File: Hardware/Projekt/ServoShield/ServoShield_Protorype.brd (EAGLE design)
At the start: 100 x 80 mm, 64 parts, among them IC0 74HCT595D, IC1 74HCT595D, IC2 74HCT595D, IC3 74HCT595D, Q1 16MHz

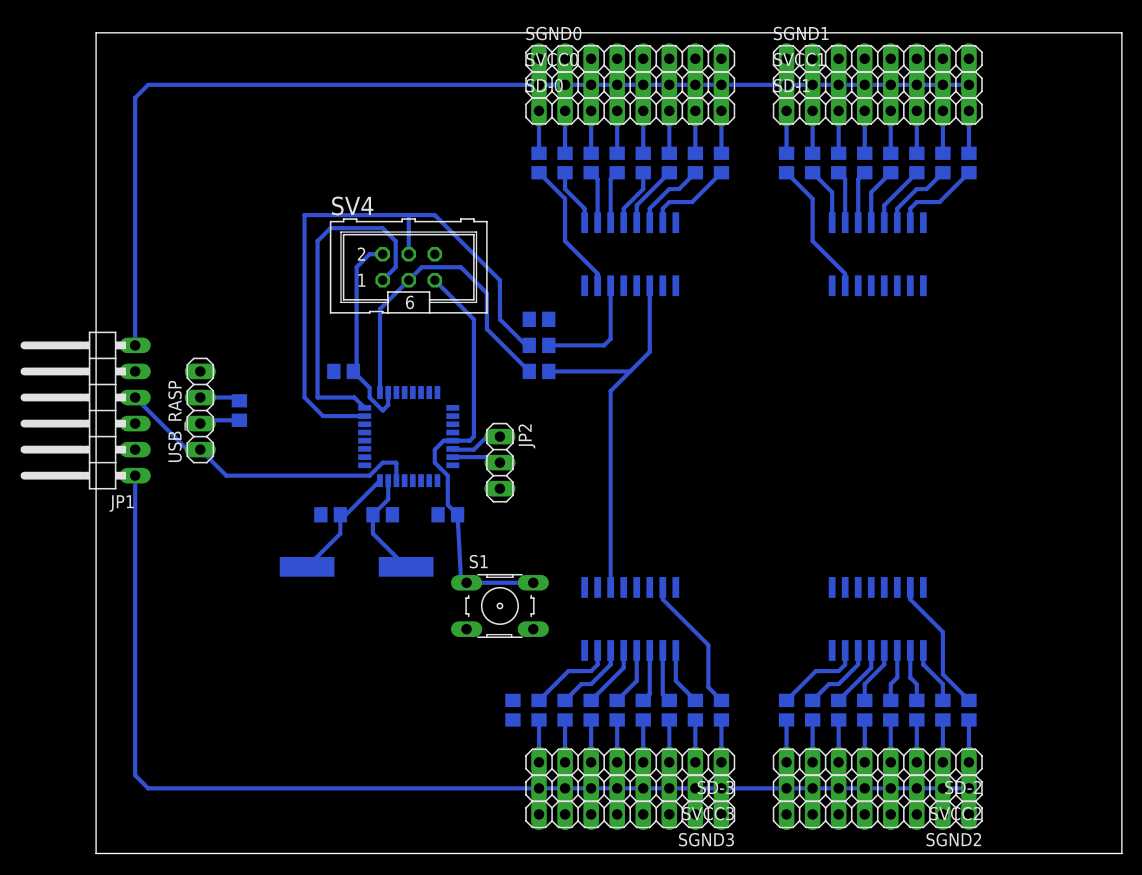
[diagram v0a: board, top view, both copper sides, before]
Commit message: Changed Pinheader and routed all signals
It is not possible to connect 8 servos on one 3x8 pinheader. The servo connectors are to wide. All 3x8 pinheader where changed for 2 3x4 pinheaders.
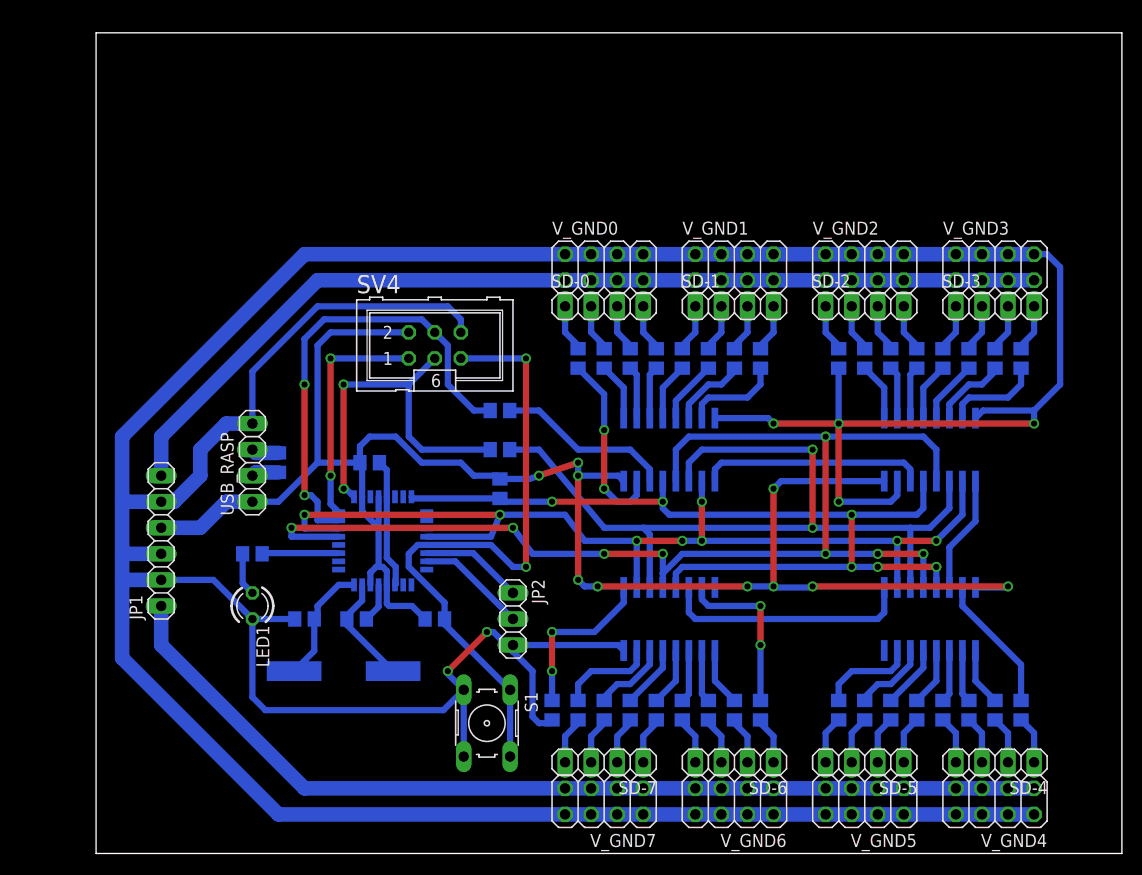
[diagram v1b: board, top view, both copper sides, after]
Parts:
- removed SGND0, SGND1, SGND2, SGND3, SVCC0, SVCC1, SVCC2, SVCC3: (no value), pinhead:1X08
- added LED1: GN_2V, led:LED3MM
- added R39: 1k5, rcl:R0805
- added SD-4, SD-5, SD-6, SD-7: (no value), pinhead:1X04
- added V_GND0, V_GND1, V_GND2, V_GND3, V_GND4, V_GND5, V_GND6, V_GND7: (no value), pinhead:2X04
- JP1: device pinhead:1X06/90 -> pinhead:1X06
- SD-0, SD-1, SD-2, SD-3: device pinhead:1X08 -> pinhead:1X04
- moved SD-3 56.9 mm to (87.6, 53.3), turned to 0 degrees
- moved SD-2 44.5 mm to (74.9, 53.3), turned to 0 degrees
- moved SD-1 23.6 mm to (62.2, 53.3)
- moved R16 19.7 mm to (74.9, 48.3)
- moved IC1 19.7 mm to (81.3, 39.4)
- moved R15 19.7 mm to (72.4, 48.3)
- moved R17 19.7 mm to (77.5, 48.3)
- moved R18 19.7 mm to (80.0, 48.3)
- moved R19 19.7 mm to (82.5, 48.3)
- moved R20 19.7 mm to (85.1, 48.3)
- moved R21 19.7 mm to (87.6, 48.3)
- moved R22 19.7 mm to (90.2, 48.3)
- moved IC0 19.4 mm to (55.9, 39.4)
- moved R10 19.4 mm to (54.6, 48.3)
- moved R7 19.4 mm to (47.0, 48.3)
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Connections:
- removed net N$23: ATMEGA328.24
- new net LED: ATMEGA328.11, R39.1
- new net N$85: LED1.A, R39.2
- net +5V/1: now also V_GND0.1, V_GND0.3, V_GND0.5, V_GND0.7, V_GND1.1, V_GND1.3, V_GND1.5, V_GND1.7, V_GND2.1, V_GND2.3, V_GND2.5, V_GND2.7, V_GND3.1, V_GND3.3, V_GND3.5, V_GND3.7; no longer SVCC0.1, SVCC0.2, SVCC0.3, SVCC0.4, SVCC0.5, SVCC0.6, SVCC0.7, SVCC0.8, SVCC1.1, SVCC1.2, SVCC1.3, SVCC1.4, SVCC1.5, SVCC1.6, SVCC1.7, SVCC1.8
- net +5V/2: now also V_GND4.1, V_GND4.3, V_GND4.5, V_GND4.7, V_GND5.1, V_GND5.3, V_GND5.5, V_GND5.7, V_GND6.1, V_GND6.3, V_GND6.5, V_GND6.7, V_GND7.1, V_GND7.3, V_GND7.5, V_GND7.7; no longer SVCC2.1, SVCC2.2, SVCC2.3, SVCC2.4, SVCC2.5, SVCC2.6, SVCC2.7, SVCC2.8, SVCC3.1, SVCC3.2, SVCC3.3, SVCC3.4, SVCC3.5, SVCC3.6, SVCC3.7, SVCC3.8
- net G: now also ATMEGA328.24; no longer ATMEGA328.12
- net GND: now also LED1.K, V_GND0.2, V_GND0.4, V_GND0.6, V_GND0.8, V_GND1.2, V_GND1.4, V_GND1.6, V_GND1.8, V_GND2.2, V_GND2.4, V_GND2.6, V_GND2.8, V_GND3.2, V_GND3.4, V_GND3.6, V_GND3.8, V_GND4.2, V_GND4.4, V_GND4.6, V_GND4.8, V_GND5.2, V_GND5.4, V_GND5.6, V_GND5.8, V_GND6.2, V_GND6.4, V_GND6.6, V_GND6.8, V_GND7.2, V_GND7.4, V_GND7.6, V_GND7.8; no longer SGND0.1, SGND0.2, SGND0.3, SGND0.4, SGND0.5, SGND0.6, SGND0.7, SGND0.8, SGND1.1, SGND1.2, SGND1.3, SGND1.4, SGND1.5, SGND1.6, SGND1.7, SGND1.8, SGND2.1, SGND2.2, SGND2.3, SGND2.4, SGND2.5, SGND2.6, SGND2.7, SGND2.8, SGND3.1, SGND3.2, SGND3.3, SGND3.4, SGND3.5, SGND3.6, SGND3.7, SGND3.8
- net N$29: now also SD-1.1; no longer SD-0.5
- net N$30: now also SD-1.2; no longer SD-0.6
- net N$31: now also SD-1.3; no longer SD-0.7
- net N$32: now also SD-1.4; no longer SD-0.8
- net N$34: now also SD-2.1; no longer SD-1.1
- net N$43: now also SD-2.2; no longer SD-1.2
- net N$44: now also SD-2.3; no longer SD-1.3
- net N$45: now also SD-2.4; no longer SD-1.4
- net N$46: now also SD-3.1; no longer SD-1.5
- net N$47: now also SD-3.2; no longer SD-1.6
- net N$48: now also SD-3.3; no longer SD-1.7
- net N$49: now also SD-3.4; no longer SD-1.8
- net N$60: now also SD-4.1; no longer SD-2.1
- net N$61: now also SD-4.2; no longer SD-2.2
- net N$62: now also SD-4.3; no longer SD-2.3
- net N$63: now also SD-4.4; no longer SD-2.4
- net N$64: now also SD-5.1; no longer SD-2.5
- net N$65: now also SD-5.2; no longer SD-2.6
- net N$66: now also SD-5.3; no longer SD-2.7
- net N$67: now also SD-5.4; no longer SD-2.8
- net N$76: now also SD-6.1; no longer SD-3.1
- net N$77: now also SD-6.2; no longer SD-3.2
- net N$78: now also SD-6.3; no longer SD-3.3
- net N$79: now also SD-6.4; no longer SD-3.4
- net N$80: now also SD-7.1; no longer SD-3.5
- net N$81: now also SD-7.2; no longer SD-3.6
- net N$82: now also SD-7.3; no longer SD-3.7
- net N$83: now also SD-7.4; no longer SD-3.8
- net N$9: now also ATMEGA328.12; no longer ATMEGA328.11
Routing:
- net GND: track 0.00 -> 423.9 mm, vias 0 -> 4
- net VCC: track 51.2 -> 175.0 mm, vias 0 -> 10
- net RCK: track 0.00 -> 119.7 mm, vias 0 -> 8
- net SCL: track 0.00 -> 97.9 mm, vias 0 -> 8
- net G: track 0.00 -> 90.0 mm, vias 0 -> 6
- net SCK1: track 38.9 -> 83.8 mm, vias 0 -> 2
- net N$53: track 0.00 -> 24.5 mm
- net N$36: track 0.00 -> 21.9 mm
- net !RST: track 41.8 -> 63.2 mm, vias 0 -> 2
- net +5V/2: track 111.0 -> 94.7 mm
- net N$52: track 0.00 -> 16.3 mm, vias 0 -> 2
- net MOSI: track 57.6 -> 45.4 mm, vias 0 -> 2
- net N$5: track 0.00 -> 11.4 mm
- net +5V/1: track 105.9 -> 95.2 mm
- net MISO: track 33.3 -> 22.9 mm, vias 0 -> 2
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
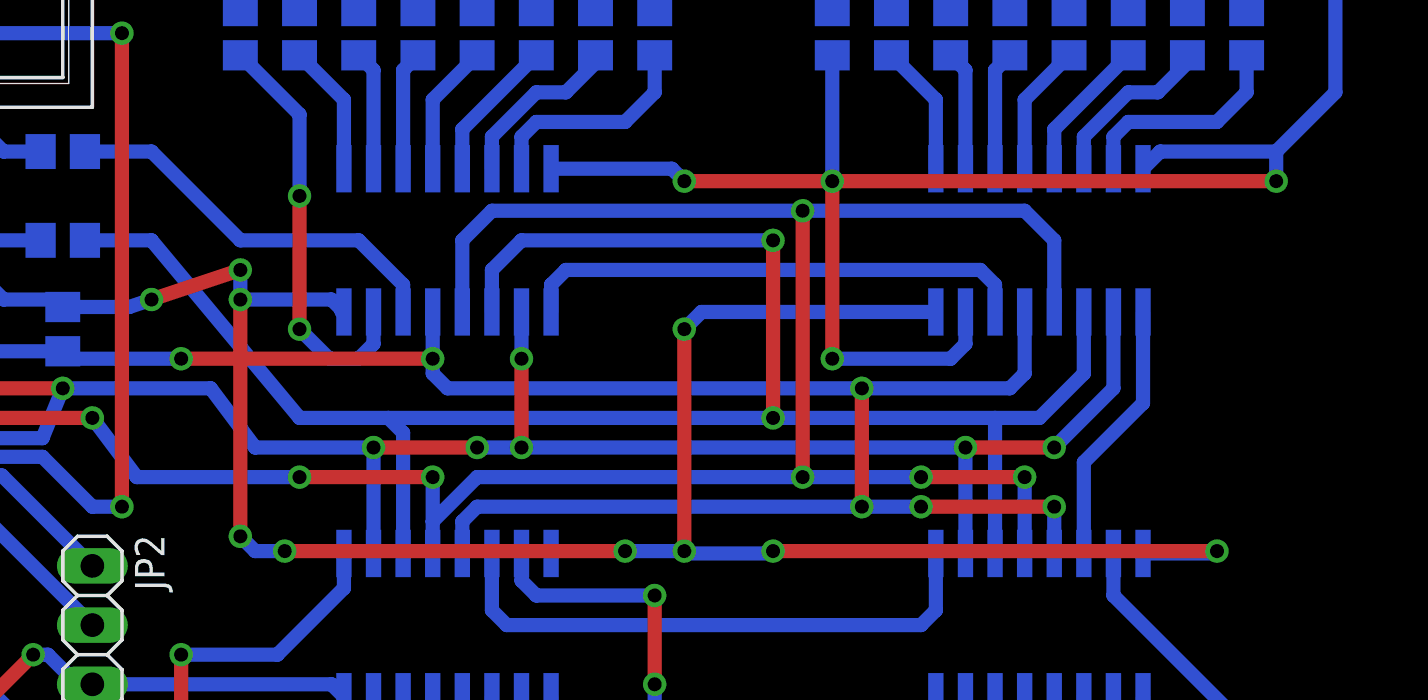
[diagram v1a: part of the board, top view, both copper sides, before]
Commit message: Corrected some overlapping routes
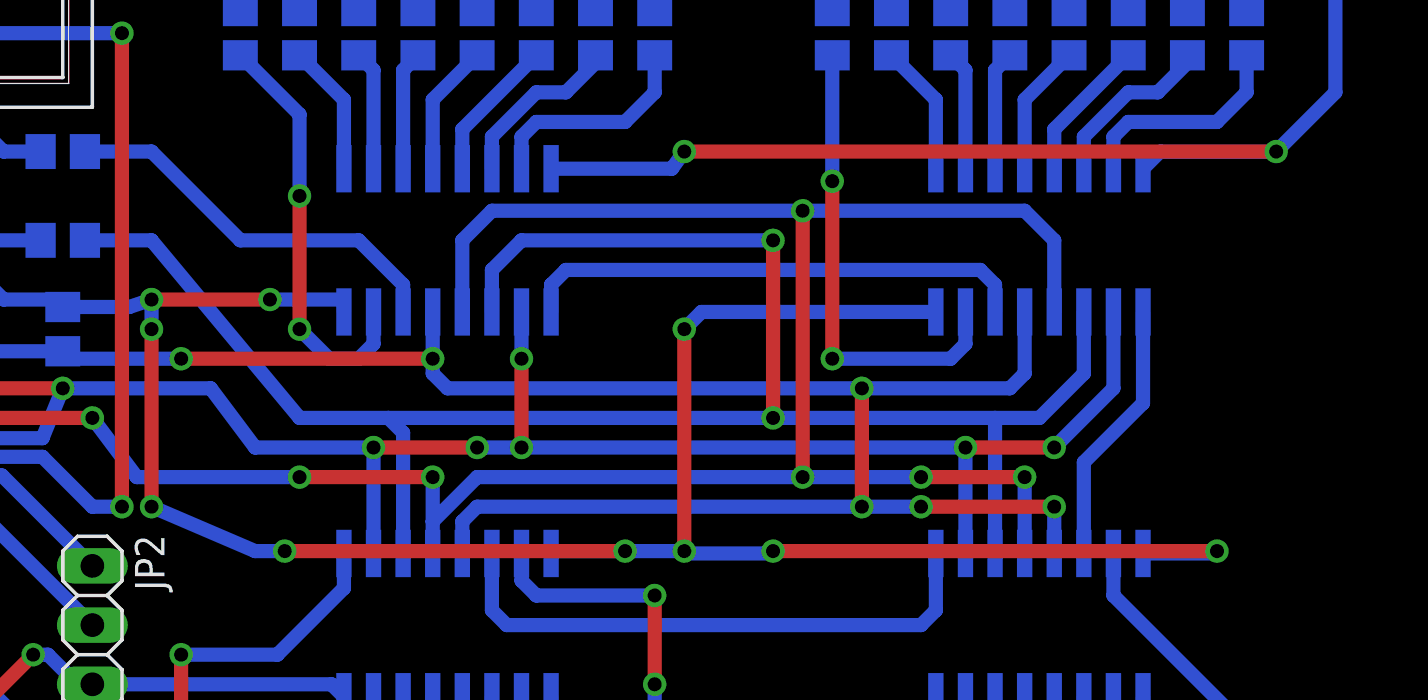
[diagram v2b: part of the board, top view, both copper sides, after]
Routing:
- net VCC: track 175.0 -> 179.7 mm
- net GND: track 423.9 -> 422.8 mm
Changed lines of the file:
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@@
 <wire x1="15.24" y1="46.99" x2="15.24" y2="41.91" width="0.6096" layer="16"/>
 <wire x1="60.325" y1="42.4434" x2="65.5066" y2="42.4434" width="0.6096" layer="16"/>
-<wire x1="65.5066" y1="42.4434" x2="66.04" y2="41.91" width="0.6096" layer="16"/>
-<via x="66.04" y="41.91" extent="1-16" drill="0.6" shape="octagon"/>
-<wire x1="91.44" y1="43.18" x2="91.44" y2="41.91" width="0.6096" layer="16"/>
-<via x="91.44" y="41.91" extent="1-16" drill="0.6" shape="octagon"/>
-<wire x1="66.04" y1="41.91" x2="91.44" y2="41.91" width="0.6096" layer="1"/>
+<wire x1="65.5066" y1="42.4434" x2="66.04" y2="43.18" width="0.6096" layer="16"/>
+<via x="66.04" y="43.18" extent="1-16" drill="0.6" shape="octagon"/>
+<via x="91.44" y="43.18" extent="1-16" drill="0.6" shape="octagon"/>
+<wire x1="66.04" y1="43.18" x2="91.44" y2="43.18" width="0.6096" layer="1"/>
 <wire x1="76.2" y1="3.81" x2="76.835" y2="19.7866" width="0" layer="19" extent="16-16"/>
 <wire x1="26.35" y1="22.86" x2="19.37" y2="22.86" width="0" layer="19" extent="16-16"/>
@@
 <wire x1="26.67" y1="40.64" x2="25.72" y2="39.69" width="0.6096" layer="16"/>
 <wire x1="25.72" y1="39.69" x2="25.72" y2="38.1" width="0.6096" layer="16"/>
-<wire x1="51.435" y1="36.2966" x2="51.3334" y2="36.2966" width="0.6096" layer="16"/>
 <wire x1="39.37" y1="36.51" x2="42.225" y2="36.51" width="0.6096" layer="16"/>
 <wire x1="42.225" y1="36.51" x2="43.18" y2="36.83" width="0.6096" layer="16"/>
 <via x="43.18" y="36.83" extent="1-16" drill="0.6" shape="octagon"/>
-<via x="46.99" y="38.1" extent="1-16" drill="0.6" shape="octagon"/>
-<wire x1="43.18" y1="36.83" x2="46.99" y2="38.1" width="0.6096" layer="1"/>
+<via x="48.26" y="36.83" extent="1-16" drill="0.6" shape="octagon"/>
+<wire x1="43.18" y1="36.83" x2="48.26" y2="36.83" width="0.6096" layer="1"/>
 <wire x1="69.7484" y1="25.9334" x2="69.85" y2="26.035" width="0.6096" layer="16"/>
 <wire x1="85.725" y1="25.9334" x2="88.7984" y2="25.9334" width="0.6096" layer="16"/>
@@
 <via x="48.895" y="26.035" extent="1-16" drill="0.6" shape="octagon"/>
 <wire x1="48.895" y1="26.035" x2="47.625" y2="26.035" width="0.6096" layer="16"/>
-<wire x1="47.625" y1="26.035" x2="46.99" y2="26.67" width="0.6096" layer="16"/>
-<via x="46.99" y="26.67" extent="1-16" drill="0.6" shape="octagon"/>
-<wire x1="46.99" y1="26.67" x2="46.99" y2="36.83" width="0.6096" layer="1"/>
-<via x="46.99" y="36.83" extent="1-16" drill="0.6" shape="octagon"/>
-<wire x1="46.99" y1="36.83" x2="50.9016" y2="36.83" width="0.6096" layer="16"/>
-<wire x1="50.9016" y1="36.83" x2="51.435" y2="36.2966" width="0.6096" layer="16"/>
-<wire x1="46.99" y1="38.1" x2="46.99" y2="36.83" width="0.6096" layer="16"/>
-<wire x1="63.5" y1="26.035" x2="60.325" y2="25.9334" width="0" layer="19" extent="16-16"/>
+<wire x1="47.625" y1="26.035" x2="43.18" y2="27.94" width="0.6096" layer="16"/>
+<via x="43.18" y="27.94" extent="1-16" drill="0.6" shape="octagon"/>
+<wire x1="43.18" y1="27.94" x2="43.18" y2="35.56" width="0.6096" layer="1"/>
+<via x="43.18" y="35.56" extent="1-16" drill="0.6" shape="octagon"/>
+<wire x1="63.5" y1="26.035" x2="60.325" y2="26.035" width="0.6096" layer="16"/>
+<wire x1="60.325" y1="26.035" x2="60.325" y2="25.9334" width="0.6096" layer="16"/>
+<wire x1="43.18" y1="35.56" x2="43.18" y2="36.83" width="0.6096" layer="16"/>
+<wire x1="48.26" y1="36.83" x2="51.435" y2="36.83" width="0.6096" layer="16"/>
+<wire x1="51.435" y1="36.83" x2="51.435" y2="36.2966" width="0.6096" layer="16"/>
 </signal>
 <signal name="N$1">

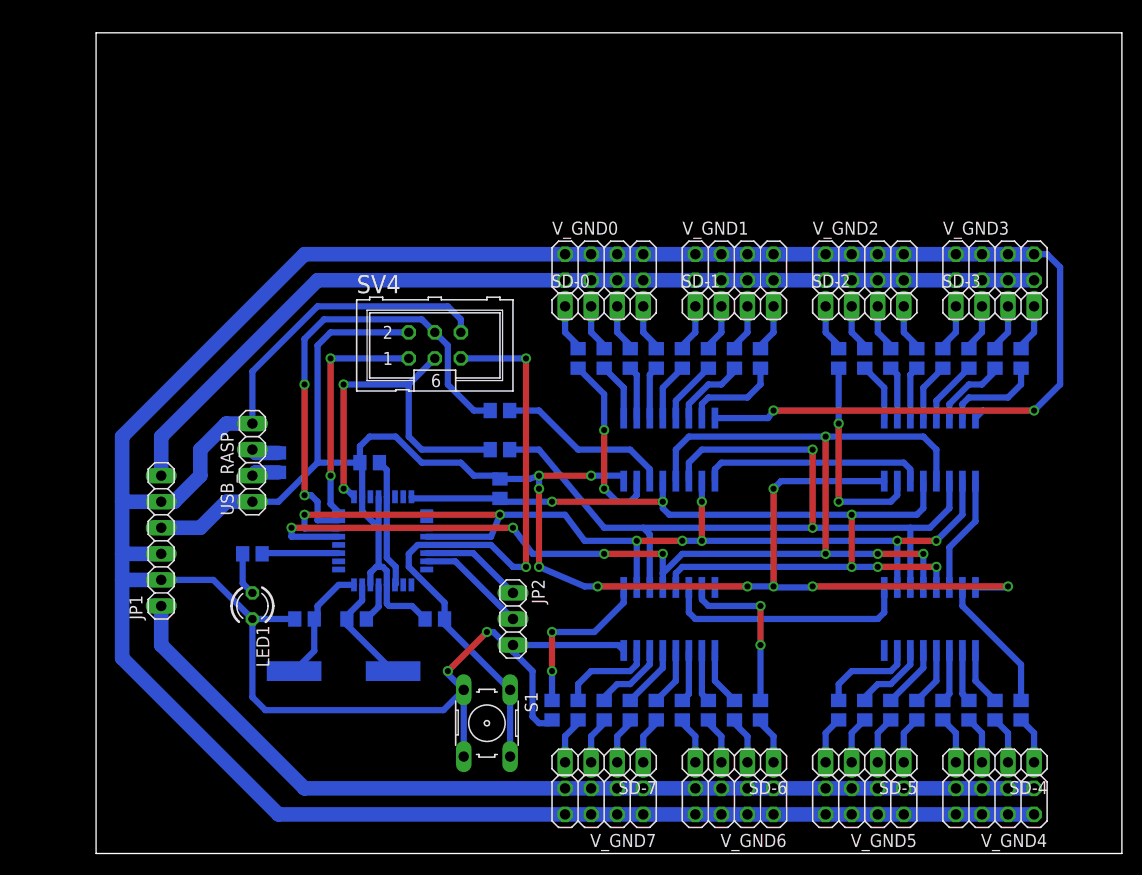
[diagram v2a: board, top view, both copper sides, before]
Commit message: Changed via diameter and routed missing signals
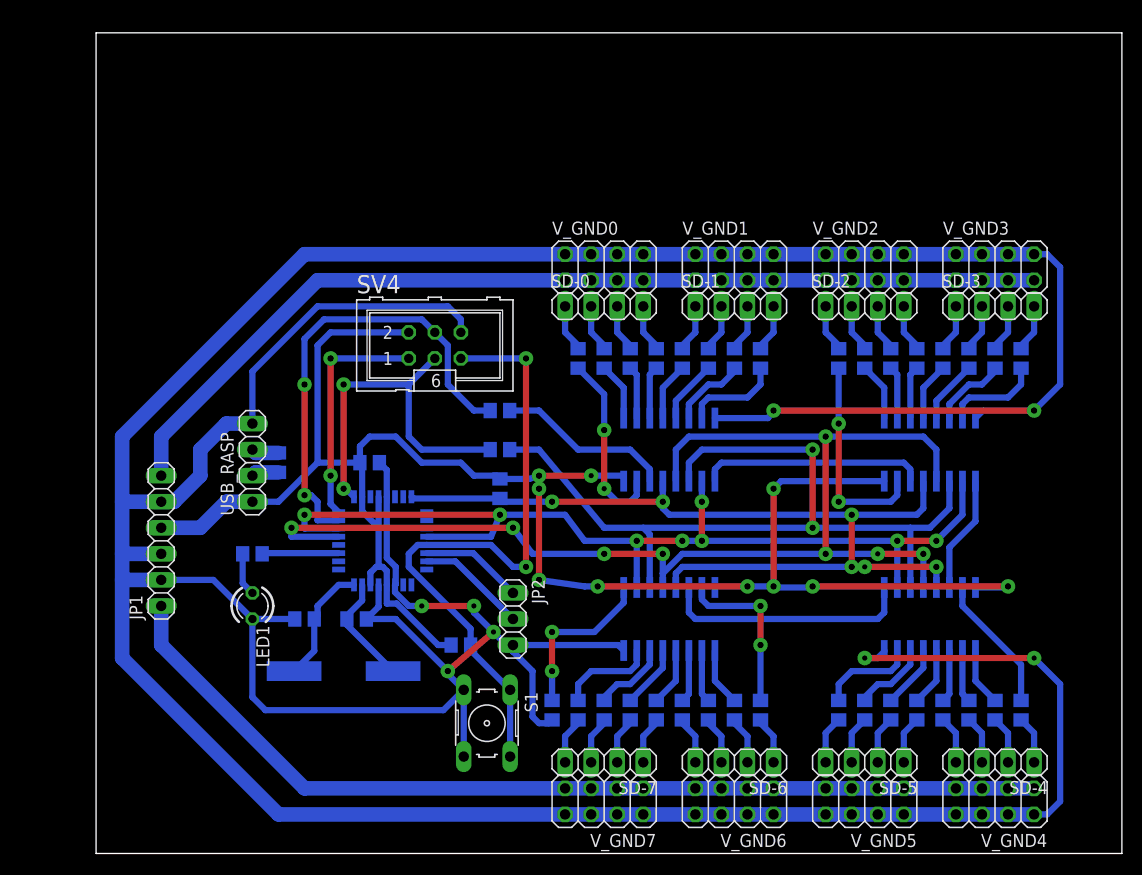
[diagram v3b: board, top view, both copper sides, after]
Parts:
- moved R1 3.59 mm to (35.6, 20.3)
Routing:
- net GND: track 422.8 -> 481.9 mm, vias 4 -> 11
- net VCC: track 179.7 -> 184.2 mm, vias 10 -> 19
- net !RST: vias 2 -> 4
- net SCL: vias 8 -> 16
- net SCK1: vias 2 -> 4
- net SCK: vias 2 -> 4
- net RCK: vias 8 -> 15
- net N$68: vias 2 -> 4
- net N$52: vias 2 -> 4
- net N$33: vias 2 -> 4
- net N$3: vias 2 -> 3
- net MOSI: vias 2 -> 4
- net MISO: vias 2 -> 4
- net G: vias 6 -> 11
